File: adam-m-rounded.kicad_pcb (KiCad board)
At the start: 2 copper layers, 114.5 x 95.3 mm, 21 parts, among them J1 AudioJack4dpb, SW1 SW_Push, SW10 SW_Push, SW11 SW_Push, SW12 SW_Push, SW13 SW_Push, SW14 SW_Push, SW15 SW_Push, SW16 SW_Push, SW17 SW_Push, SW2 SW_Push, SW3 SW_Push, SW4 SW_Push, SW5 SW_Push, SW6 SW_Push, SW7 SW_Push, SW8 SW_Push, SW9 SW_Push, U1 ProMicro-kbd

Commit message: add gerbers
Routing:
- net gnd: track 526.2 -> 486.7 mm
- net Switch11: track 175.4 -> 172.3 mm
- net Switch6: track 143.2 -> 140.3 mm
- net Switch10: track 159.0 -> 156.5 mm
- net Switch2: track 119.0 -> 116.5 mm
- net Switch13: track 85.0 -> 82.8 mm
- net Switch3: track 96.7 -> 94.5 mm
- net Switch15: track 137.6 -> 135.5 mm
- net Switch9: track 90.4 -> 88.4 mm
- net Switch4: track 71.1 -> 69.1 mm
- net Switch14: track 110.4 -> 108.6 mm
- net Switch12: track 62.5 -> 60.8 mm
- net Switch1: track 127.3 -> 125.7 mm
- net Switch8: track 66.6 -> 65.1 mm
- net Switch5: track 49.1 -> 47.8 mm
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
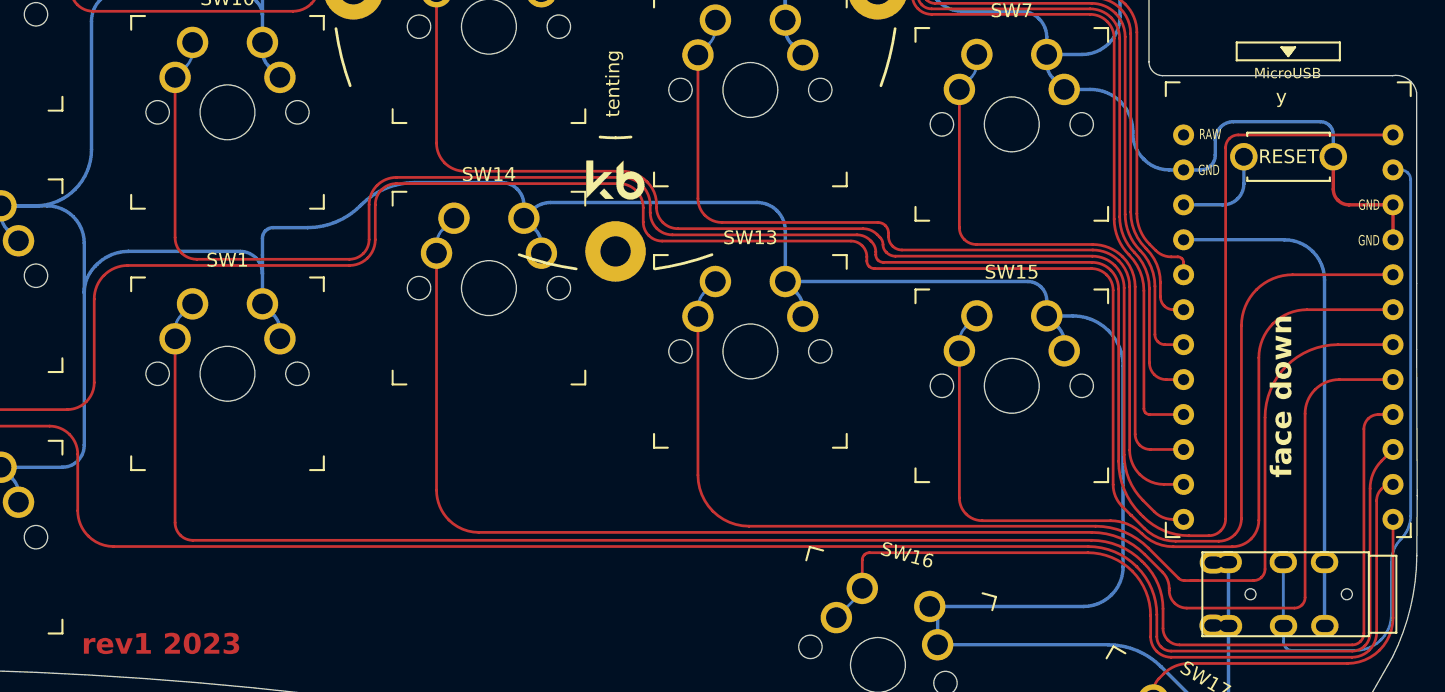
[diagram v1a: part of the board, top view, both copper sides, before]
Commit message: fix footprint for mcu
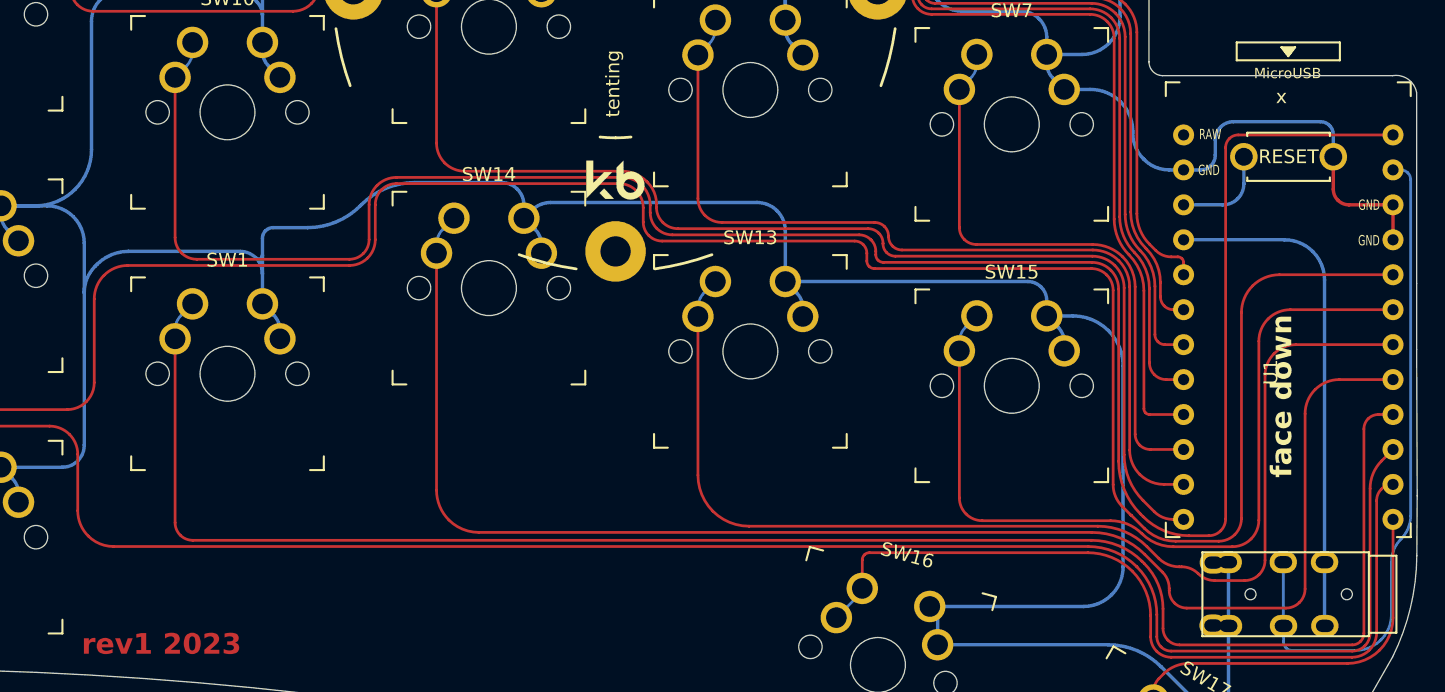
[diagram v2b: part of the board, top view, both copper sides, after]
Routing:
- net gnd: track 486.7 -> 487.3 mm
- net Switch11: track 172.3 -> 172.9 mm
- net Switch12: track 60.8 -> 61.3 mm

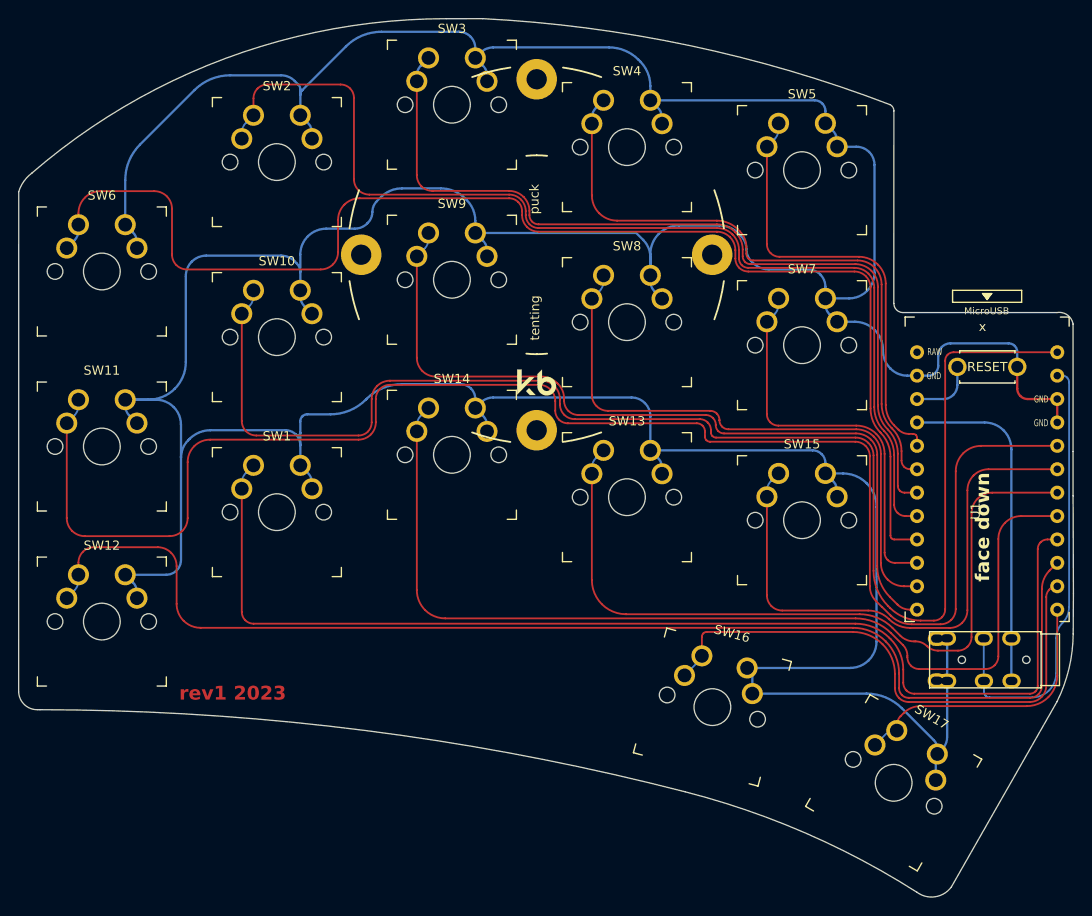
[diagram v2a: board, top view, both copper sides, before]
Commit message: Tweaks for ERC
- Removed silkscreen from pads of microcontroller, switch
- Moved trace closest to board edge to under microcontroller
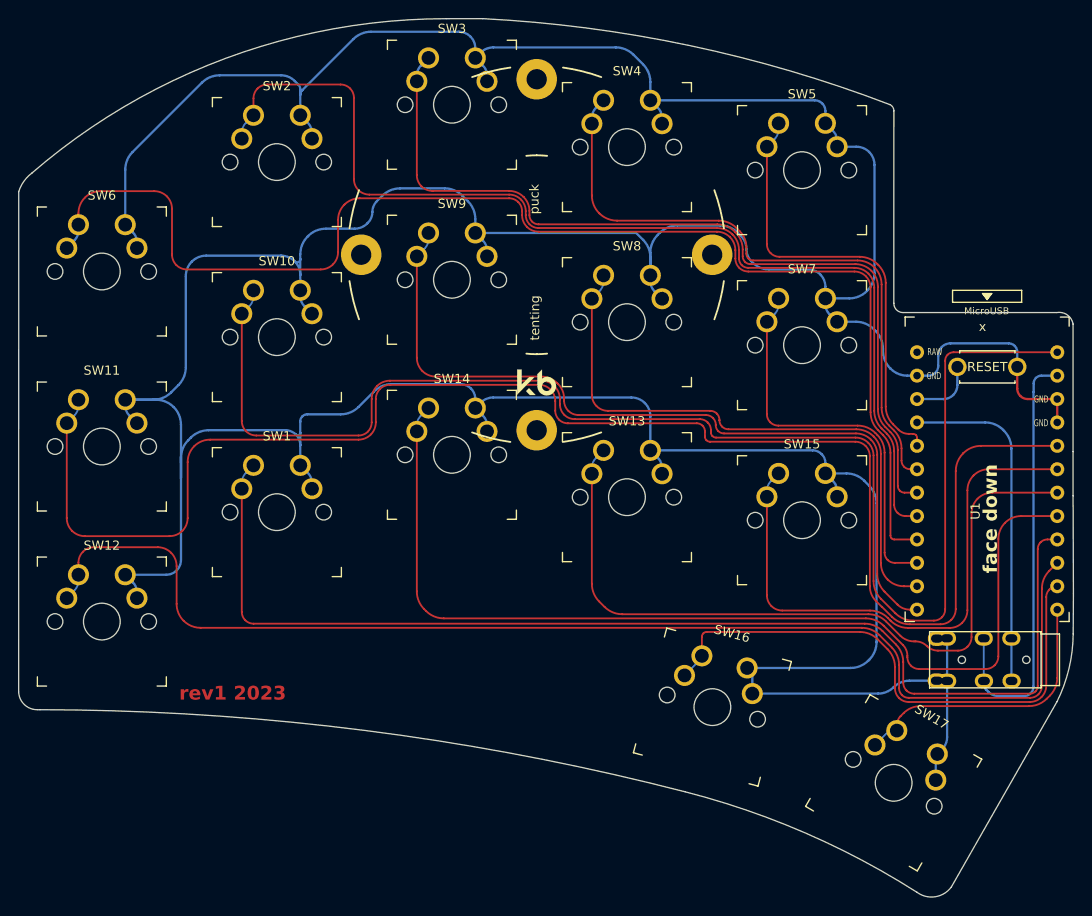
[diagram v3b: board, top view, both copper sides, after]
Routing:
- net gnd: track 487.3 -> 523.8 mm
- net Switch18: track 48.5 -> 47.5 mm
- net Switch10: track 156.5 -> 157.4 mm
- net Switch15: track 135.5 -> 136.3 mm
- net Switch1: track 125.7 -> 126.5 mm
- net Switch13: track 83.1 -> 84.0 mm
- net Switch14: track 108.3 -> 109.1 mm
- net Switch4: track 69.1 -> 69.8 mm
- net Switch3: track 94.5 -> 95.3 mm
- net Switch9: track 88.5 -> 89.3 mm
- net Switch6: track 140.3 -> 141.1 mm
- net Switch2: track 116.5 -> 117.3 mm
- net Switch12: track 61.3 -> 62.0 mm
- net Switch5: track 47.8 -> 48.4 mm
- net Switch7: track 42.4 -> 43.1 mm
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
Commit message: update
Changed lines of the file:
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@@
         (effects (font (size 1 1) (thickness 0.15)))
     )
-    (fp_text value "ProMicro-kbd" (at -1.27 14.732) (layer "F.Fab")
-        (effects (font (size 1 1) (thickness 0.15)))
+    (fp_text value "ProMicro-kbd" (at -0.6 13.4) (layer "F.SilkS")
+        (effects (font (size 0.75 0.75) (thickness 0.15)))
     )
-    (fp_text user "GND" (at 5.86 -6.77) (layer "B.SilkS")
+    (fp_text user "GND" (at -5.77 -11.88) (layer "B.SilkS")
         (effects (font (size 0.75 0.5) (thickness 0.125)) (justify mirror))
     )
-    (fp_text user "GND" (at -5.77 -11.88) (layer "B.SilkS")
+    (fp_text user "GND" (at 5.88 -9.35) (layer "B.SilkS")
         (effects (font (size 0.75 0.5) (thickness 0.125)) (justify mirror))
     )
@@
         (effects (font (size 0.75 0.5) (thickness 0.125)) (justify mirror))
     )
-    (fp_text user "x" (at -1.2065 -16.256) (layer "B.SilkS")
-        (effects (font (size 1 1) (thickness 0.15)) (justify mirror))
-    )
-    (fp_text user "GND" (at 5.88 -9.35) (layer "B.SilkS")
+    (fp_text user "GND" (at 5.86 -6.77) (layer "B.SilkS")
         (effects (font (size 0.75 0.5) (thickness 0.125)) (justify mirror))
     )
-    (fp_text user "MicroUSB" (at -0.05 -18.95) (layer "F.SilkS")
-        (effects (font (size 0.75 0.75) (thickness 0.12)))
-    )
-    (fp_text user "x" (at -0.5 -17.25) (layer "F.SilkS")
-        (effects (font (size 1 1) (thickness 0.15)))
+    (fp_text user "RAW" (at -5.67 -14.52) (layer "F.SilkS")
+        (effects (font (size 0.75 0.5) (thickness 0.125)))
     )
     (fp_text user "GND" (at -5.77 -11.91) (layer "F.SilkS")
-        (effects (font (size 0.75 0.5) (thickness 0.125)))
-    )
-    (fp_text user "RAW" (at -5.67 -14.52) (layer "F.SilkS")
         (effects (font (size 0.75 0.5) (thickness 0.125)))
     )
@@
     (fp_line (start -8.9 14.75) (end -7.9 14.75)
       (stroke (width 0.15) (type solid)) (layer "F.SilkS"))
-    (fp_line (start -3.75 -21.2) (end -3.75 -19.9)
-      (stroke (width 0.15) (type solid)) (layer "F.SilkS"))
-    (fp_line (start -3.75 -19.9) (end 3.75 -19.9)
-      (stroke (width 0.15) (type solid)) (layer "F.SilkS"))
-    (fp_line (start -0.5 -20.85) (end 0.5 -20.85)
-      (stroke (width 0.15) (type solid)) (layer "F.SilkS"))
-    (fp_line (start -0.35 -20.7) (end 0.35 -20.7)
-      (stroke (width 0.15) (type solid)) (layer "F.SilkS"))
-    (fp_line (start -0.25 -20.55) (end 0.25 -20.55)
-      (stroke (width 0.15) (type solid)) (layer "F.SilkS"))
-    (fp_line (start -0.15 -20.4) (end 0.15 -20.4)
-      (stroke (width 0.15) (type solid)) (layer "F.SilkS"))
-    (fp_line (start 0 -20.2) (end -0.5 -20.85)
-      (stroke (width 0.15) (type solid)) (layer "F.SilkS"))
-    (fp_line (start 0.5 -20.85) (end 0 -20.2)
-      (stroke (width 0.15) (type solid)) (layer "F.SilkS"))
-    (fp_line (start 3.75 -21.2) (end -3.75 -21.2)
-      (stroke (width 0.15) (type solid)) (layer "F.SilkS"))
-    (fp_line (start 3.75 -19.9) (end 3.75 -21.2)
-      (stroke (width 0.15) (type solid)) (layer "F.SilkS"))
     (fp_line (start 8.9 -18.3) (end 7.95 -18.3)
       (stroke (width 0.15) (type solid)) (layer "F.SilkS"))
@@
     (fp_line (start -8.9 14.75) (end -8.9 -18.3)
       (stroke (width 0.15) (type solid)) (layer "F.Fab"))
-    (fp_line (start -3.75 -19.6) (end -3.75 -18.299039)
-      (stroke (width 0.15) (type solid)) (layer "F.Fab"))
-    (fp_line (start -3.75 -19.6) (end 3.75 -19.6)
-      (stroke (width 0.15) (type solid)) (layer "F.Fab"))
     (fp_line (start -3.75 -18.3) (end 3.75 -18.3)
       (stroke (width 0.15) (type solid)) (layer "F.Fab"))
-    (fp_line (start 3.75 -19.6) (end 3.75 -18.3)
-      (stroke (width 0.15) (type solid)) (layer "F.Fab"))
     (fp_line (start 3.76 -18.3) (end 8.9 -18.3)

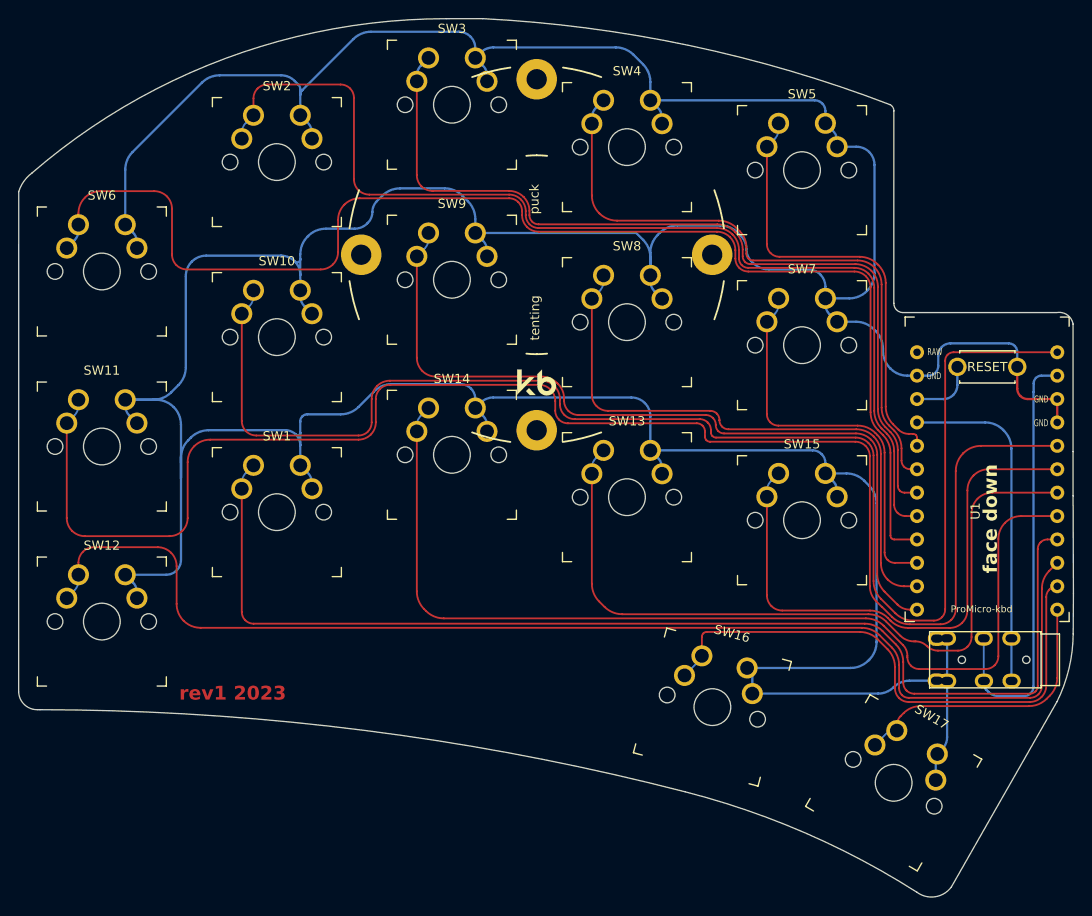
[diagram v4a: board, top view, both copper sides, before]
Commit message: more rounding, straighter lines, bit more text
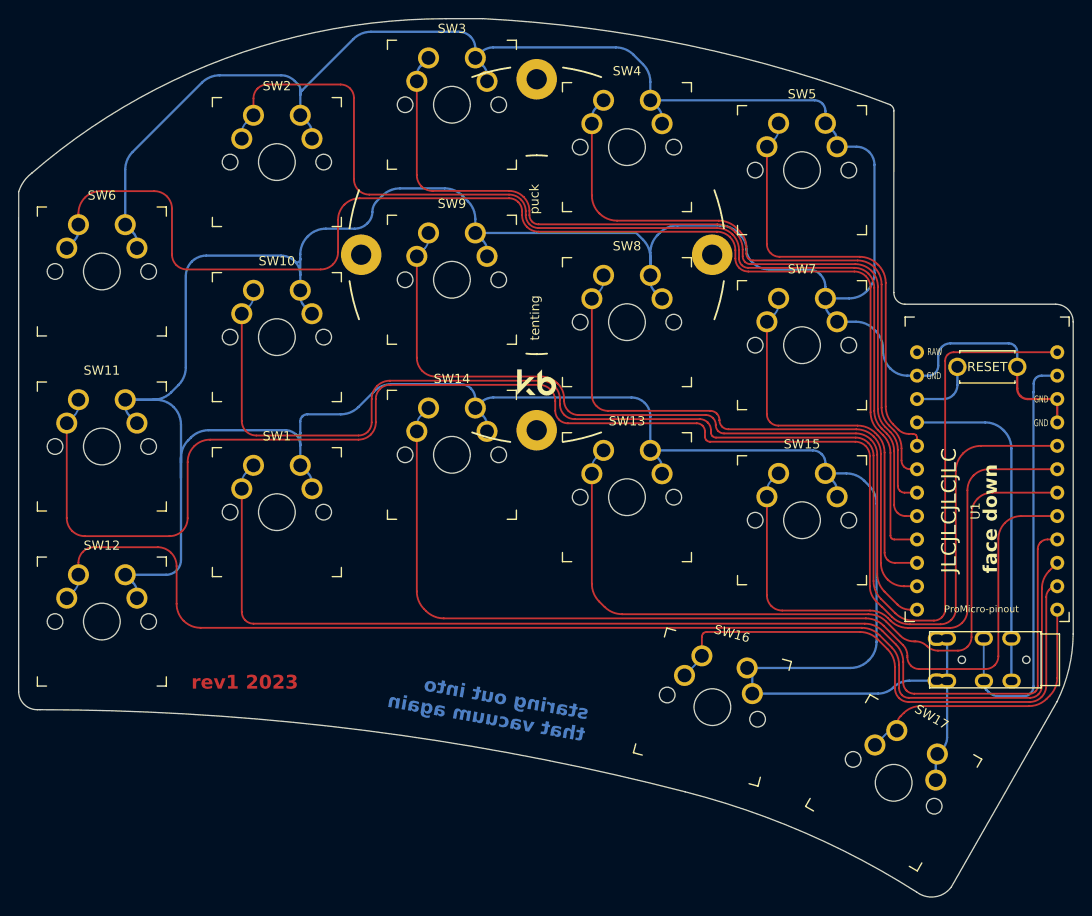
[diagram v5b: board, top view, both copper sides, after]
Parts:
- U1: value ProMicro-kbd -> ProMicro-pinout
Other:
- outline, holes or cut-outs redrawn
- board text added: "JLCJLCJLCJLC"
- board text added: "staring out into that vacuum again"

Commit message: rework switch numbering, rearrange schematic for clarity
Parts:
- renumbered SW6 to SW1, SW7 to SW10, SW12 to SW11, SW1 to SW12, SW14 to SW13, SW13 to SW14, SW11 to SW6, SW10 to SW7, SW9 to SW8, SW8 to SW9
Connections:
- SW1 pad 1: Switch6 -> Switch1
- SW10 pad 1: Switch7 -> Switch10
- SW11 pad 1: Switch15 -> Switch11
- SW12 pad 1: Switch1 -> Switch12
- SW13 pad 1: Switch14 -> Switch13
- SW14 pad 1: Switch13 -> Switch14
- SW15 pad 1: Switch12 -> Switch15
- SW6 pad 1: Switch11 -> Switch6
- SW7 pad 1: Switch10 -> Switch7
- SW8 pad 1: Switch9 -> Switch8
- SW9 pad 1: Switch8 -> Switch9
- U1 pad 1: Switch10 -> Switch7
- U1 pad 10: Switch15 -> Switch11
- U1 pad 13: Switch9 -> Switch8
- U1 pad 14: Switch8 -> Switch9
- U1 pad 15: Switch7 -> Switch10
- U1 pad 16: Switch6 -> Switch1
- U1 pad 5: Switch11 -> Switch6
- U1 pad 6: Switch12 -> Switch15
- U1 pad 7: Switch13 -> Switch14
- U1 pad 8: Switch14 -> Switch13
- U1 pad 9: Switch1 -> Switch12
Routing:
- net Switch7: track 43.1 -> 157.4 mm
- net Switch10: track 157.4 -> 43.1 mm
- net Switch15: track 136.3 -> 62.0 mm
- net Switch12: track 62.0 -> 126.5 mm
- net Switch11: track 173.5 -> 136.3 mm
- net Switch6: track 141.1 -> 173.5 mm
- net Switch14: track 109.1 -> 84.0 mm
- net Switch13: track 84.0 -> 109.1 mm
- net Switch9: track 89.3 -> 65.6 mm
- net Switch8: track 65.6 -> 89.3 mm
- net Switch1: track 126.5 -> 141.1 mm

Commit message: Re-assign TRRS pad labels
This is a hacked symbol anyway, may as well make it a logical one. Now
the pad order flows from one end to another of the internal
connections (note that sleeve connection is at opposite end to pin so
*appears* out-of-order on PCB footprint). Also explicitly include pads
that are shorted together by reversible footprint and reflect this in
schematic.
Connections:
- J1 pad B: Switch18 -> vcc
- J1 pad C: gnd -> Data
- J1 pad D: vcc -> gnd
- U1 pad 2: Switch18 -> Data
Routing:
- net Data: track 0.00 -> 47.5 mm
- net Switch18: track 47.5 -> 0.00 mm
